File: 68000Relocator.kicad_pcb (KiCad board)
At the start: 2 copper layers, 97.8 x 97 mm, 2 parts, among them U1 68000D, U2 68000D

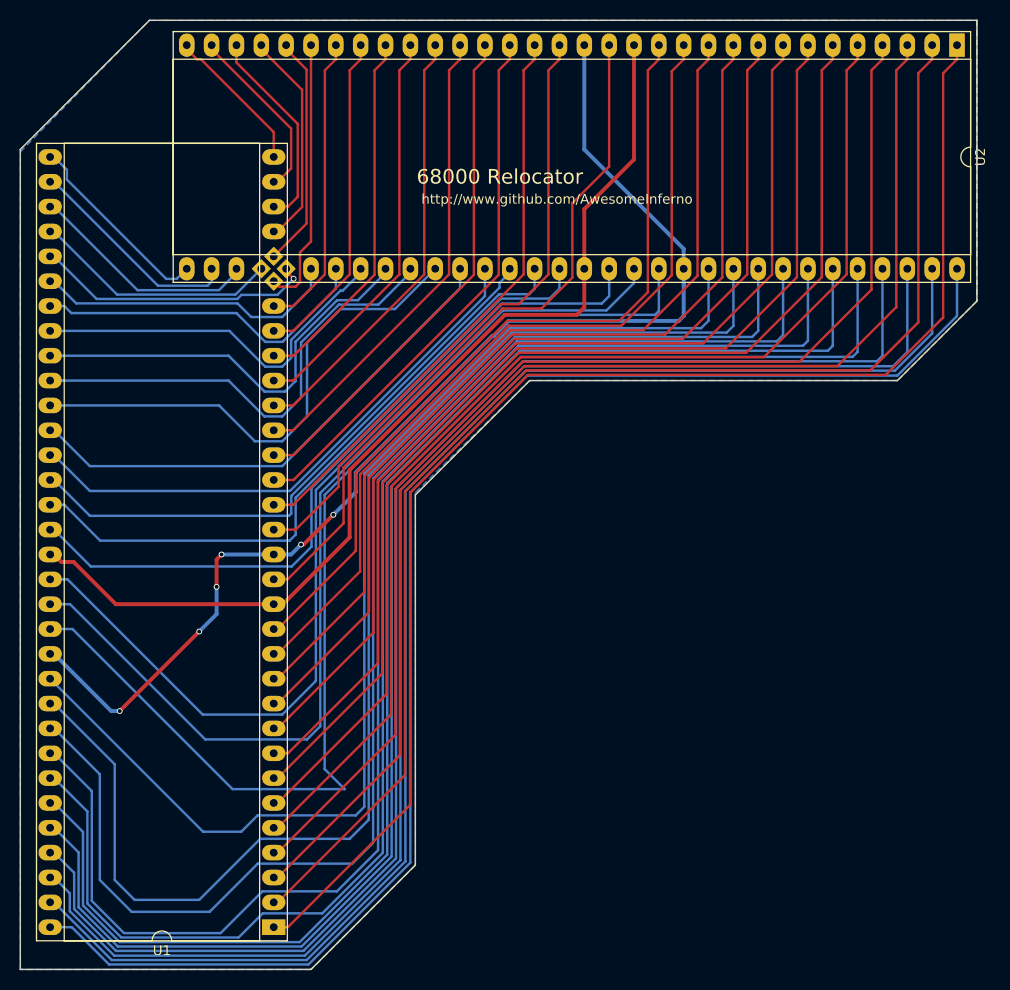
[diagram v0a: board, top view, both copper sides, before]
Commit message: Change Vcc plane to ground plane, stitch planes & other minor tweaks
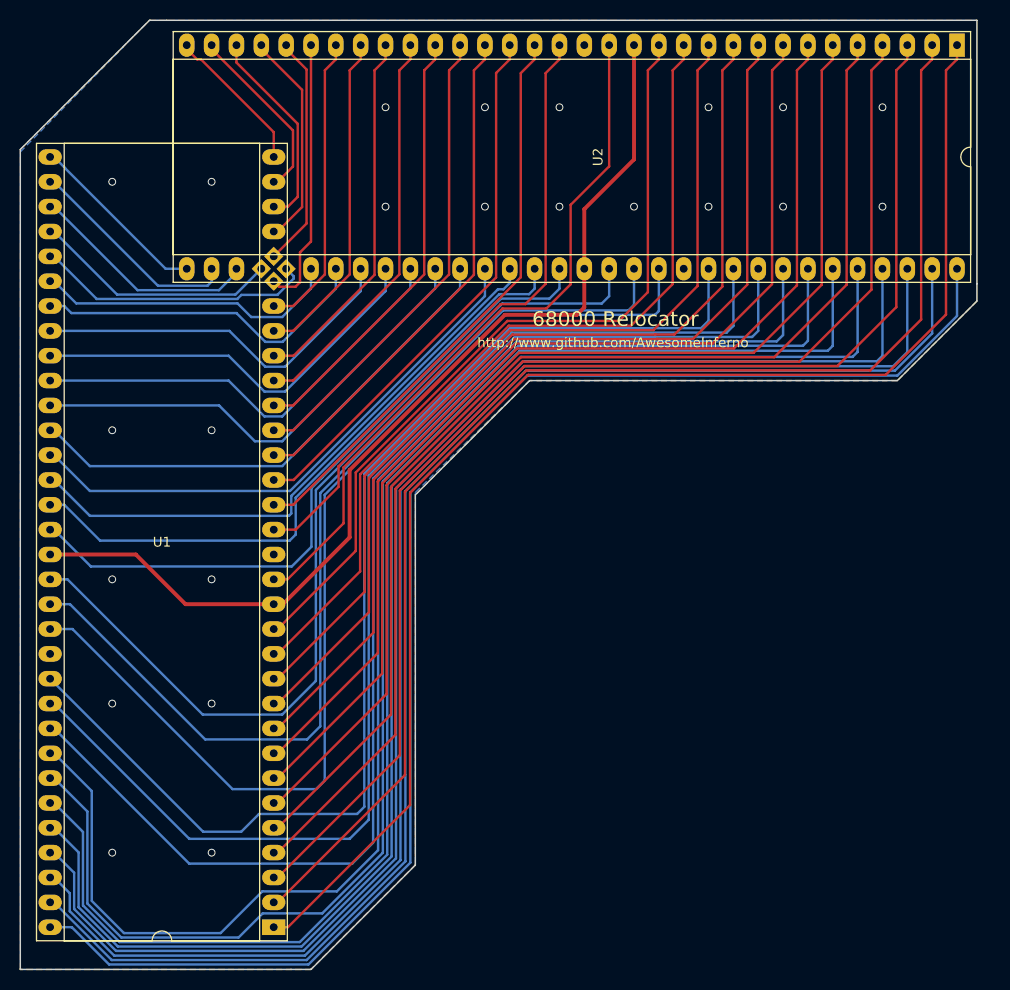
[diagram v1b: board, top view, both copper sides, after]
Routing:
- net GND: track 120.7 -> 0.00 mm, vias 6 -> 23
- net /D14: track 136.2 -> 124.1 mm
- net /D13: track 139.6 -> 129.2 mm
- net /A23: track 114.5 -> 111.1 mm
- net /A15: track 52.6 -> 49.4 mm
- net /A14: track 48.3 -> 45.9 mm
- net /A5: track 20.1 -> 18.7 mm
- net /A22: track 100.6 -> 101.9 mm
- net /A13: track 44.0 -> 42.7 mm
- net /D0: track 119.5 -> 120.1 mm
- net /R/W: track 100.7 -> 101.3 mm
- net /BG: track 92.1 -> 92.7 mm
- net /BGACK: track 86.6 -> 87.1 mm
- net /DTACK: track 96.2 -> 96.7 mm
- net /A9: track 28.9 -> 29.1 mm, vias 1 -> 0
- added copper zone on F.Cu, net GND
- removed copper zone on F.Cu, net VCC
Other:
- net class PWR: clearance 0.3 -> 0.2; trace_width 0.4 -> 0.5; via_dia 0.6 -> 0.8; via_drill 0.4 -> 0.6
- rule pad_to_mask_clearance: 0.2 -> 0

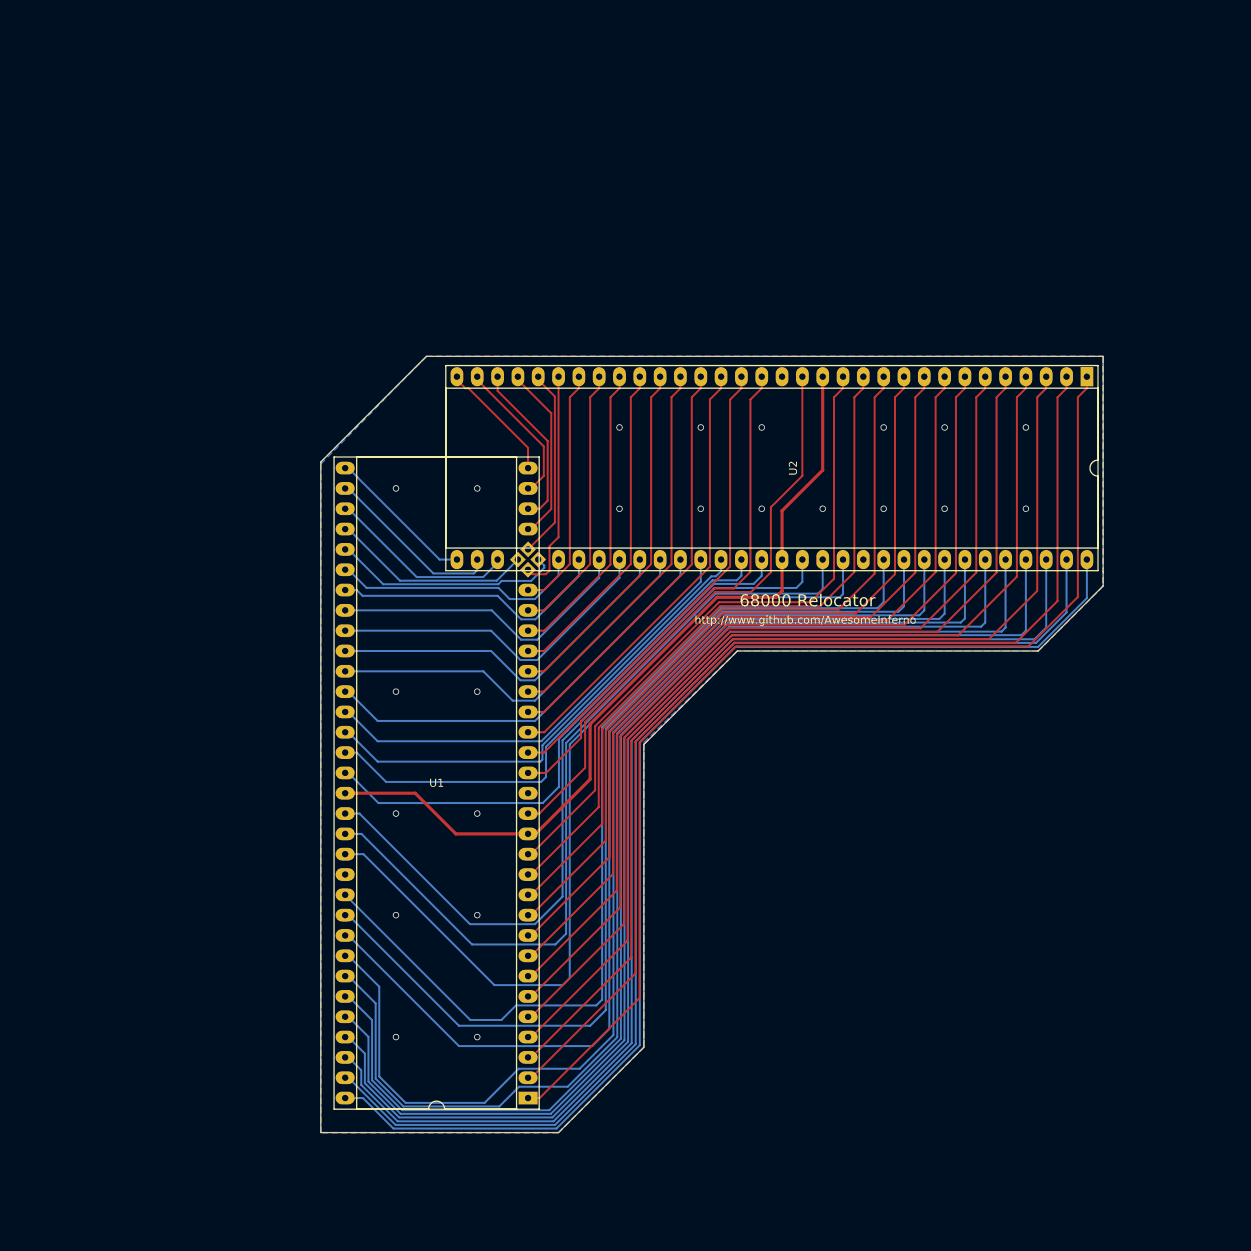
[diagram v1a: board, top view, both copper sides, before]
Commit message: Try to avoid crashing into the A500 Kickstart ROM
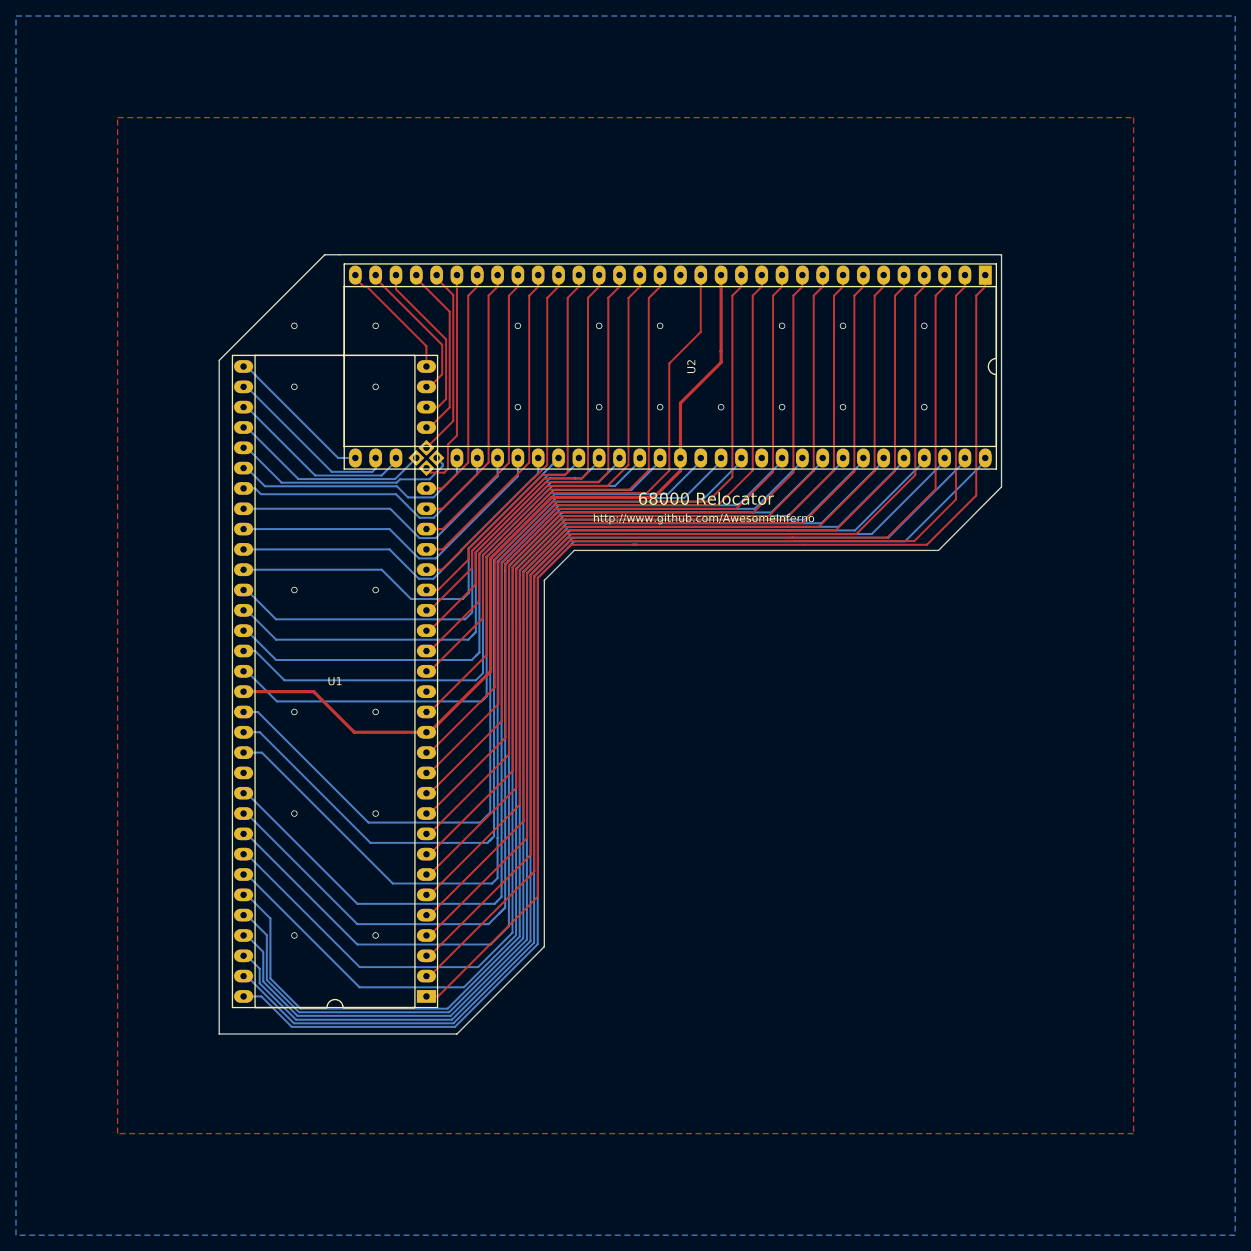
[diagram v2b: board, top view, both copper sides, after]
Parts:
- moved U1 18.0 mm to (115.1, 140.0)
- moved U2 18.0 mm to (184.9, 49.8)
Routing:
- net /D12: track 143.8 -> 134.1 mm
- net /A21: track 95.2 -> 102.9 mm
- net /A20: track 71.5 -> 78.6 mm
- net /D11: track 145.0 -> 138.2 mm
- net /A18: track 60.9 -> 67.0 mm
- net /D3: track 136.3 -> 142.0 mm
- net /D4: track 141.8 -> 147.2 mm
- net /A19: track 66.4 -> 71.4 mm
- net /D1: track 125.5 -> 130.1 mm
- net /D2: track 130.9 -> 135.5 mm
- net /BR: track 82.9 -> 87.5 mm
- net /BGACK: track 87.1 -> 91.8 mm
- net /BG: track 92.7 -> 97.3 mm
- net /DTACK: track 96.7 -> 101.3 mm
- net /R/W: track 101.3 -> 105.9 mm
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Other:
- board size 97.8 x 97 mm -> 97.8 x 97.4 mm
